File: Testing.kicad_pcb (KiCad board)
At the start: 2 copper layers, 60.5 x 25.9 mm, 18 parts, among them J4 Jack-DC, J6 In Sleeve, J7 Out Sleeve

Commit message: why does this fail DRC??
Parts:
- removed C1: 100nF, Capacitor_THT:C_Rect_L7.2mm_W2.5mm_P5.00mm_FKS2_FKP2_MKS2_MKP2
- added 100nF: 100nF, Capacitor_THT:C_Rect_L7.2mm_W2.5mm_P5.00mm_FKS2_FKP2_MKS2_MKP2, F.Cu at (172.2, 110.0)
- 1N4739A: renamed from D1; value 1N47xxA -> 1N4739A
- moved 10uF 31.2 mm to (195.3, 106.9)
- moved BS170 31.0 mm to (164.1, 107.4)
- moved 1M 7.62 mm to (181.6, 103.4), turned to 270 degrees
- moved C5k 1.30 mm to (159.5, 96.5)
- moved 4.7k 0.25 mm to (187.7, 111.0)
- moved A50k 0.25 mm to (196.3, 96.8)
- renumbered R2 to 1M, R1 to 1M, R4 to 4.7k, R3 to 5.1k
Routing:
- net Net-(C2-Pad2): track 61.2 -> 12.7 mm
- net Net-(D1-Pad2): track 69.6 -> 33.8 mm
- net Net-(C1-Pad1): track 53.6 -> 30.9 mm
- net Net-(J5-Pad1): track 26.4 -> 38.2 mm
- net +9V: track 0.00 -> 8.88 mm
- net Net-(C2-Pad1): track 44.7 -> 41.0 mm
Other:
- board size 60.5 x 25.9 mm -> 52.1 x 25.9 mm

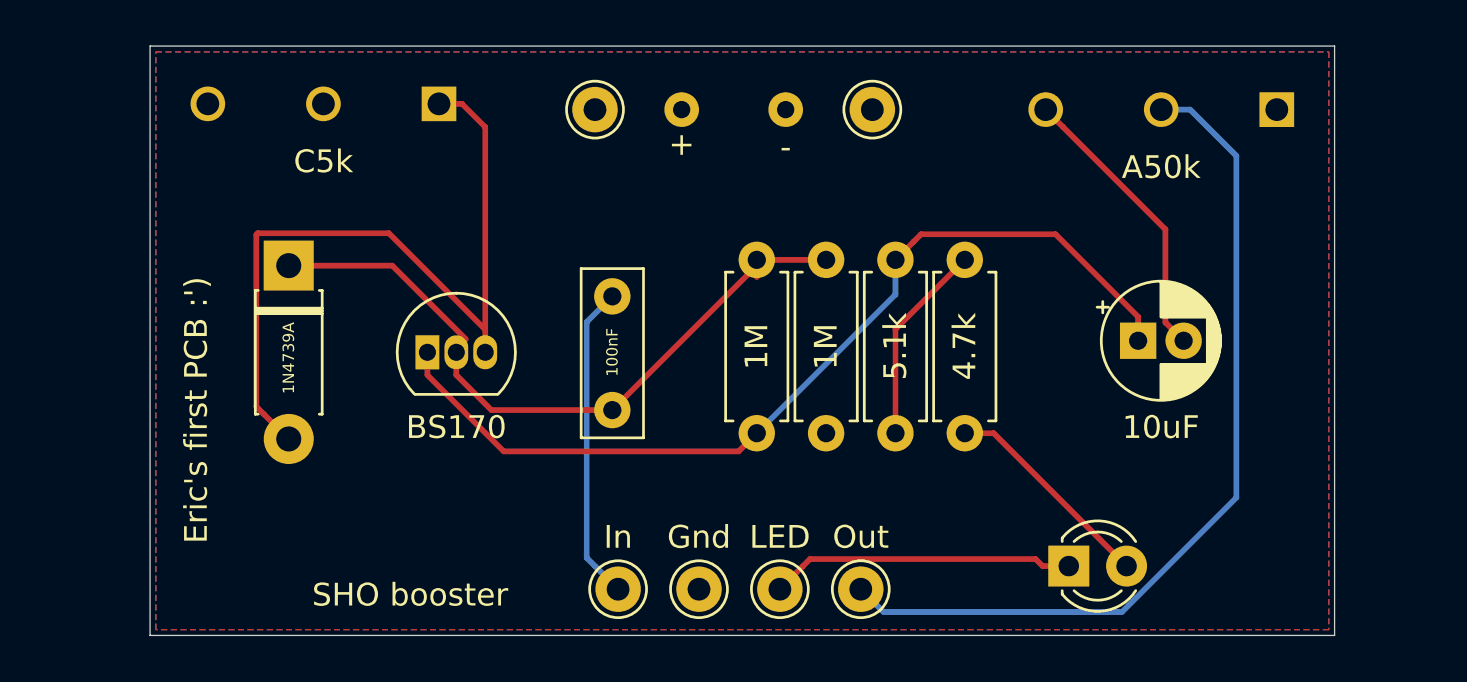
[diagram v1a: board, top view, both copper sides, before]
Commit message: Updated routing
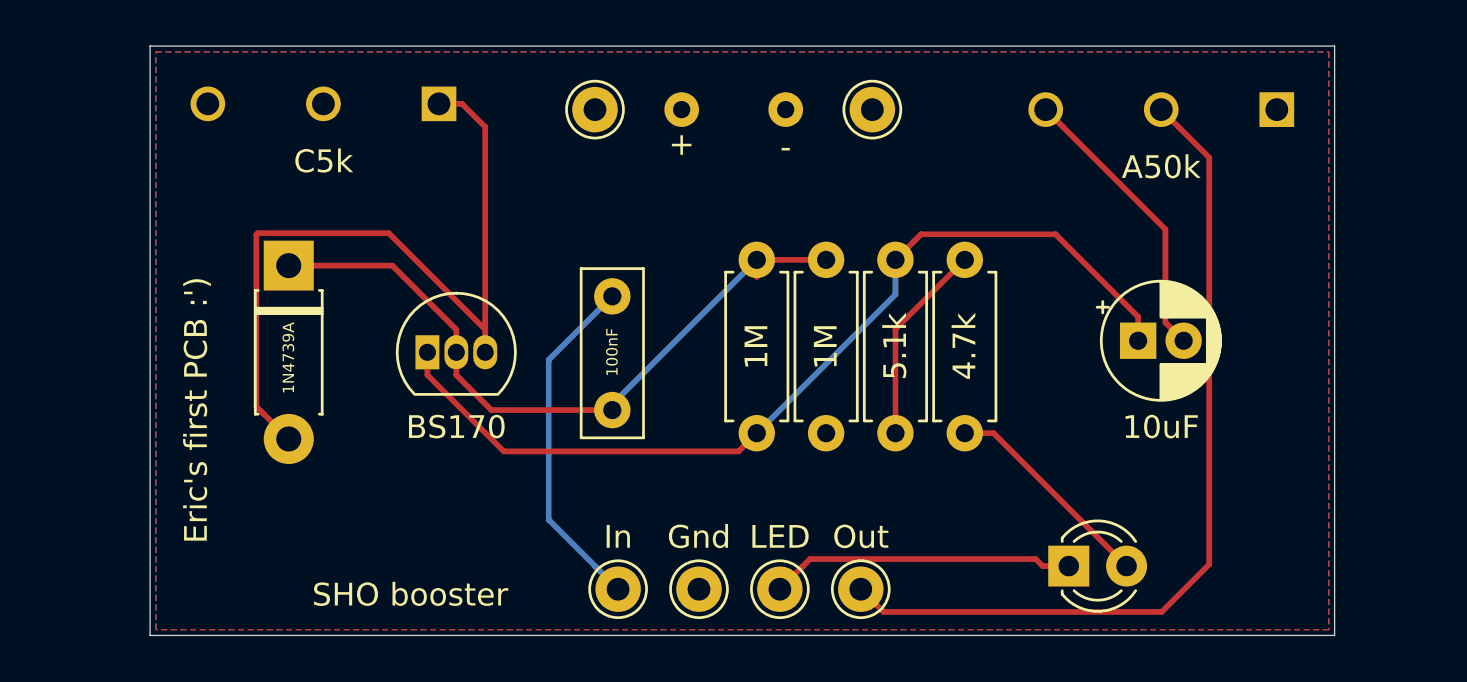
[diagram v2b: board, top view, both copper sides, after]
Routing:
- net Net-(C1-Pad2): track 13.9 -> 15.3 mm
- net Net-(J5-Pad1): track 38.2 -> 37.5 mm
- net Net-(C1-Pad1): track 30.9 -> 31.6 mm
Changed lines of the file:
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@@
     (thickness 1.6)
     (drawings 6)
-    (tracks 57)
+    (tracks 59)
     (zones 0)
     (modules 18)
@@
   (gr_line (start 203.962 93.98) (end 203.962 119.888) (layer Edge.Cuts) (width 0.05))
   (gr_line (start 151.892 93.98) (end 151.892 119.888) (layer Edge.Cuts) (width 0.05))
-  (segment (start 162.541075 103.632) (end 165.77399 106.864915) (width 0.25) (layer F.Cu) (net 1))
-  (segment (start 157.988 103.632) (end 162.541075 103.632) (width 0.25) (layer F.Cu) (net 1))
   (segment (start 177.762001 111.797999) (end 178.562 110.998) (width 0.25) (layer F.Cu) (net 2))
   (segment (start 185.457999 102.578001) (end 184.658 103.378) (width 0.25) (layer F.Cu) (net 2))
@@
   (segment (start 165.354 107.442) (end 165.354 108.442) (width 0.25) (layer F.Cu) (net 1))
   (segment (start 178.562 103.632) (end 178.562 103.378) (width 0.25) (layer F.Cu) (net 1))
-  (segment (start 172.212 109.982) (end 178.562 103.632) (width 0.25) (layer F.Cu) (net 1))
+  (segment (start 165.354 106.442) (end 165.354 107.442) (width 0.25) (layer F.Cu) (net 1))
+  (segment (start 162.544 103.632) (end 165.354 106.442) (width 0.25) (layer F.Cu) (net 1))
+  (segment (start 157.988 103.632) (end 162.544 103.632) (width 0.25) (layer F.Cu) (net 1))
+  (segment (start 172.212 109.728) (end 172.212 109.982) (width 0.25) (layer B.Cu) (net 1))
+  (segment (start 178.562 103.378) (end 172.212 109.728) (width 0.25) (layer B.Cu) (net 1))
   (segment (start 184.658 104.902) (end 178.562 110.998) (width 0.25) (layer B.Cu) (net 2))
   (segment (start 184.658 103.378) (end 184.658 104.902) (width 0.25) (layer B.Cu) (net 2))
@@
   (segment (start 184.658 110.998) (end 184.658 106.426) (width 0.25) (layer F.Cu) (net 6))
   (segment (start 171.466001 116.856001) (end 172.466 117.856) (width 0.25) (layer B.Cu) (net 8))
-  (segment (start 171.086999 106.107001) (end 171.086999 116.476999) (width 0.25) (layer B.Cu) (net 8))
-  (segment (start 171.086999 116.476999) (end 171.466001 116.856001) (width 0.25) (layer B.Cu) (net 8))
-  (segment (start 172.212 104.982) (end 171.086999 106.107001) (width 0.25) (layer B.Cu) (net 8))
+  (segment (start 169.418 114.808) (end 171.466001 116.856001) (width 0.25) (layer B.Cu) (net 8))
+  (segment (start 169.418 107.776) (end 169.418 114.808) (width 0.25) (layer B.Cu) (net 8))
+  (segment (start 172.212 104.982) (end 169.418 107.776) (width 0.25) (layer B.Cu) (net 8))
   (segment (start 194.818 116.72463) (end 194.818 116.84) (width 0.25) (layer F.Cu) (net 9))
   (segment (start 188.976 110.998) (end 194.818 116.84) (width 0.25) (layer F.Cu) (net 9))
@@
   (segment (start 192.278 116.84) (end 191.128 116.84) (width 0.25) (layer F.Cu) (net 10))
   (segment (start 192.278 116.84) (end 192.532 116.586) (width 0.25) (layer B.Cu) (net 10))
-  (segment (start 199.644 113.827002) (end 194.615003 118.855999) (width 0.25) (layer B.Cu) (net 11))
-  (segment (start 184.133999 118.855999) (end 183.134 117.856) (width 0.25) (layer B.Cu) (net 11))
-  (segment (start 199.644 98.806) (end 199.644 113.827002) (width 0.25) (layer B.Cu) (net 11))
-  (segment (start 197.612 96.774) (end 199.644 98.806) (width 0.25) (layer B.Cu) (net 11))
-  (segment (start 194.615003 118.855999) (end 184.133999 118.855999) (width 0.25) (layer B.Cu) (net 11))
-  (segment (start 196.342 96.774) (end 197.612 96.774) (width 0.25) (layer B.Cu) (net 11))
+  (segment (start 197.103999 97.535999) (end 196.342 96.774) (width 0.25) (layer F.Cu) (net 11))
+  (segment (start 198.451001 98.883001) (end 197.103999 97.535999) (width 0.25) (layer F.Cu) (net 11))
+  (segment (start 198.451001 116.762999) (end 198.451001 98.883001) (width 0.25) (layer F.Cu) (net 11))
+  (segment (start 196.358001 118.855999) (end 198.451001 116.762999) (width 0.25) (layer F.Cu) (net 11))
+  (segment (start 184.133999 118.855999) (end 196.358001 118.855999) (width 0.25) (layer F.Cu) (net 11))
+  (segment (start 183.134 117.856) (end 184.133999 118.855999) (width 0.25) (layer F.Cu) (net 11))
   (zone (net 6) (net_name +9V) (layer F.Cu) (hatch edge 0.508)
     (connect_pads (clearance 0.508))

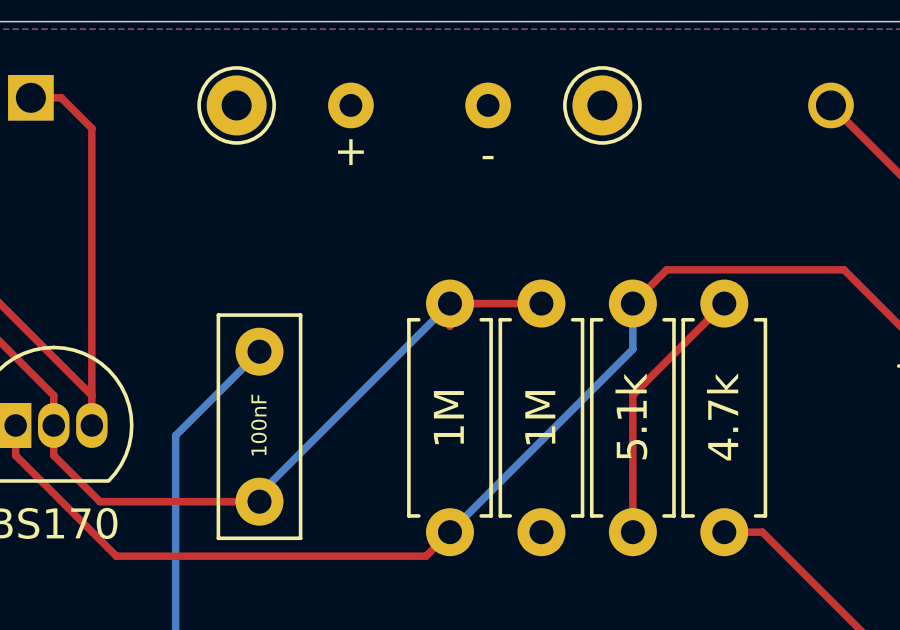
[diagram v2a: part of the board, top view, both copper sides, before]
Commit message: Remove vestigial trace
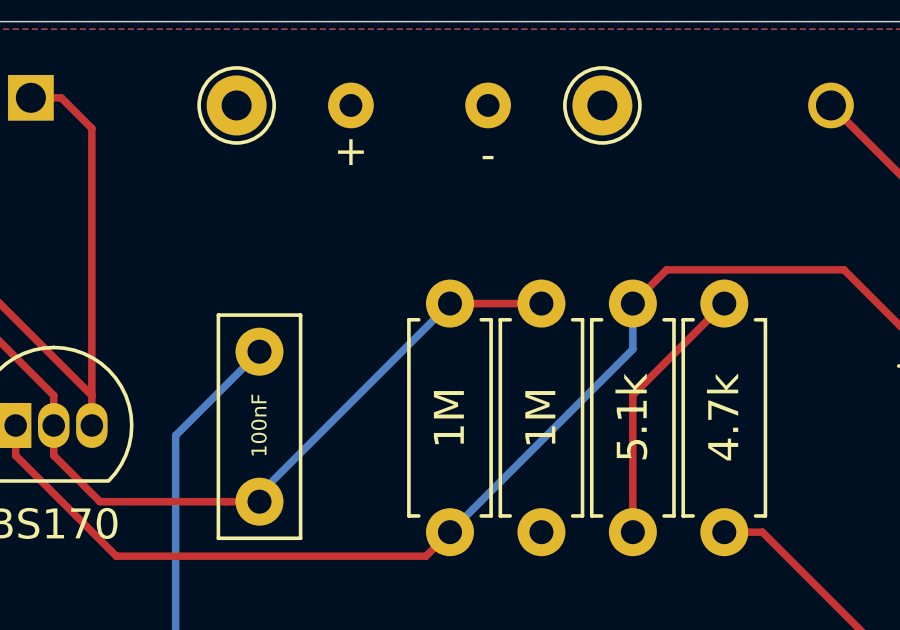
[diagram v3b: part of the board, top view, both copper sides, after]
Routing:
- net Net-(C1-Pad1): track 31.6 -> 30.8 mm
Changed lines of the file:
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@@
     (thickness 1.6)
     (drawings 6)
-    (tracks 59)
+    (tracks 58)
     (zones 0)
     (modules 18)
@@
   (segment (start 164.084 108.442) (end 167.439999 111.797999) (width 0.25) (layer F.Cu) (net 2))
   (segment (start 167.439999 111.797999) (end 177.762001 111.797999) (width 0.25) (layer F.Cu) (net 2))
-  (segment (start 178.562 104.14) (end 178.562 103.378) (width 0.25) (layer F.Cu) (net 1))
   (segment (start 172.212 109.728) (end 172.212 109.982) (width 0.25) (layer F.Cu) (net 1))
   (segment (start 178.562 103.378) (end 181.61 103.378) (width 0.25) (layer F.Cu) (net 1))
